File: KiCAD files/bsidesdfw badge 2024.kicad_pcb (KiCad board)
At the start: 2 copper layers, 117.4 x 117.4 mm, 29 parts, among them Q1 BC548, SW1 SW_SPDT_312, U1 NE555P, U2 74HC595

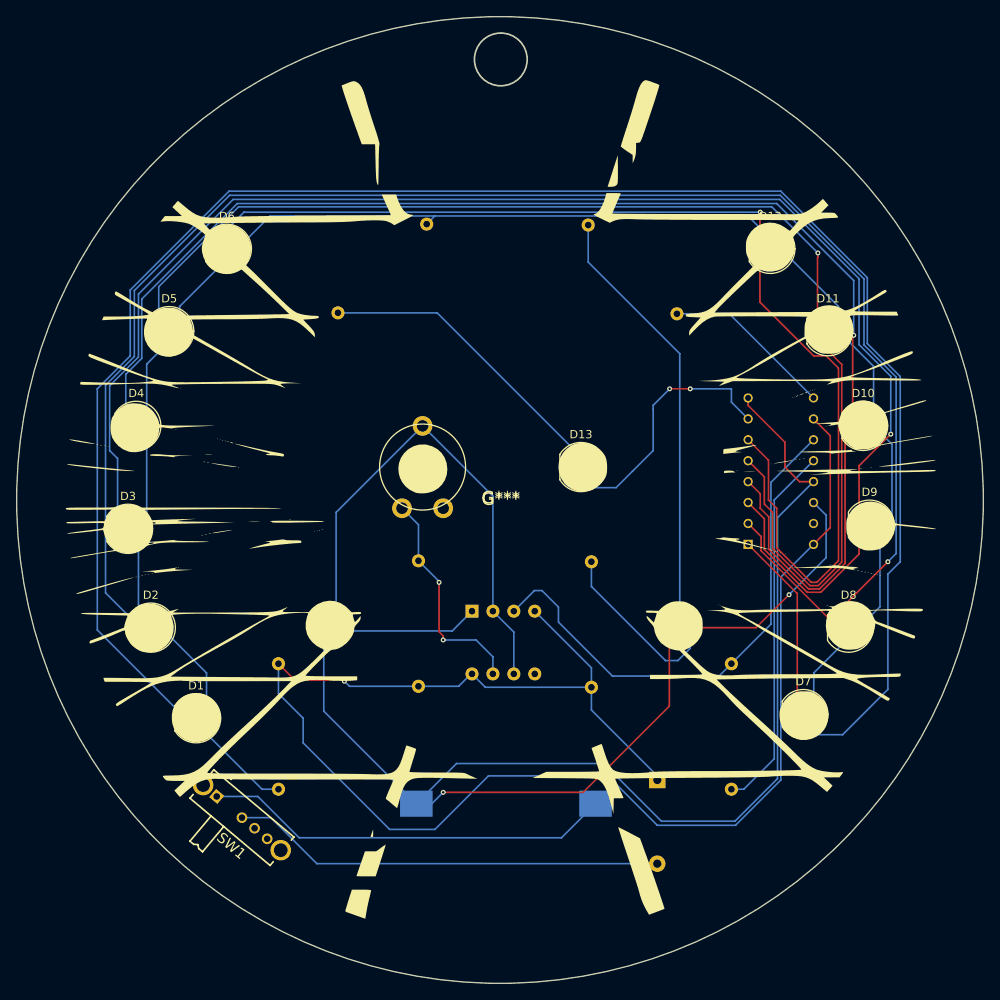
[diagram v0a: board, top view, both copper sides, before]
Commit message: gerbers for PCBWay; Added BSides Logo and website; added silkscreen credits for badge contributors. Moved LED footprints to back of board to address silkscreen conflicts, details are in the README.md
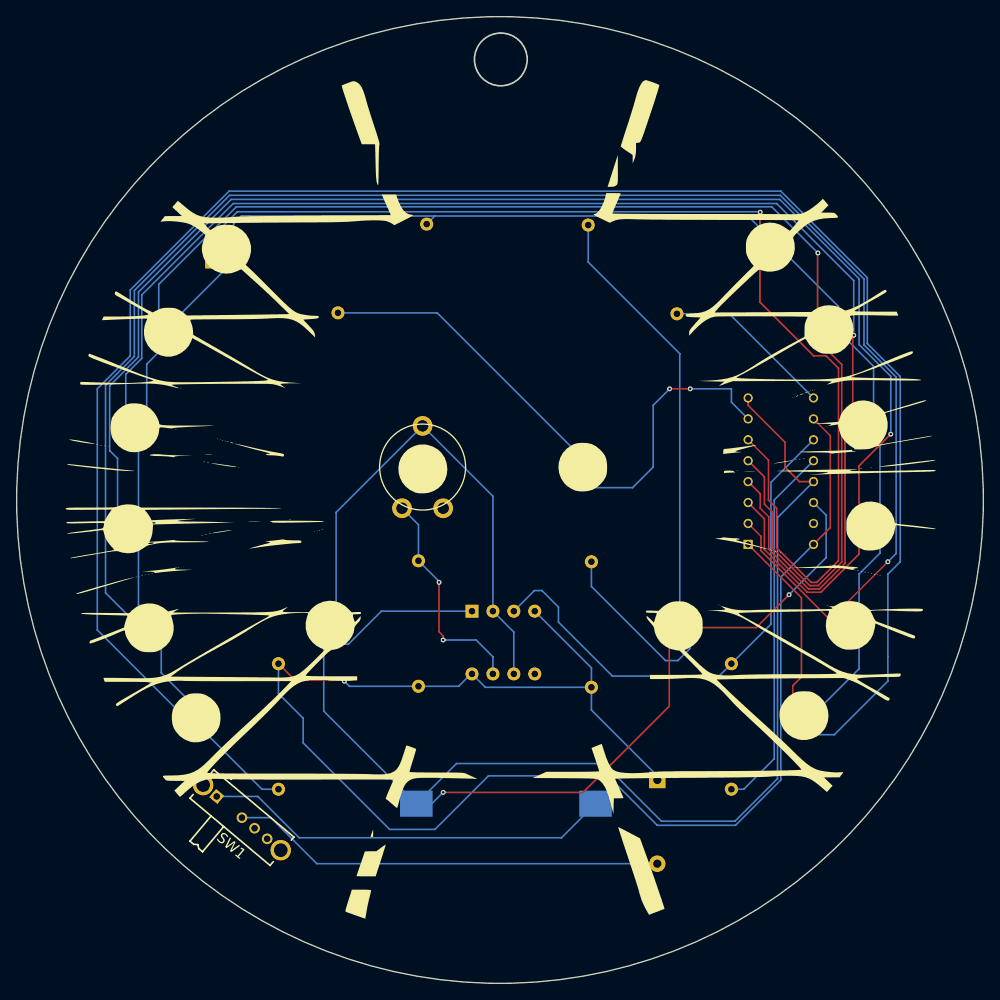
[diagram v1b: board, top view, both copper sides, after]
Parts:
- added G***: LOGO, hon1nbo-library:bsides-logo, B.Cu at (138.0, 50.5)
- added G***: LOGO, hon1nbo-library:hon1nbo-soberdogs-art, B.Cu at (106.5, 91.5)
- D1, D10, D11, D12, D13, D2, D3, D4, D5, D6, D7, D8, D9: moved to B.Cu
- moved D6 1.57 mm to (102.5, 67.5)
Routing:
- net Net-(D12-K): track 140.6 -> 142.8 mm
- net Net-(D13-K): track 33.8 -> 34.4 mm
- net Net-(D1-A): track 215.8 -> 216.4 mm
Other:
- board text added: "Design: ibi5 Masking: bearsinports Electrical & PCB: hon1nbo"
- board text added: "https://bsidesdfw.com/"

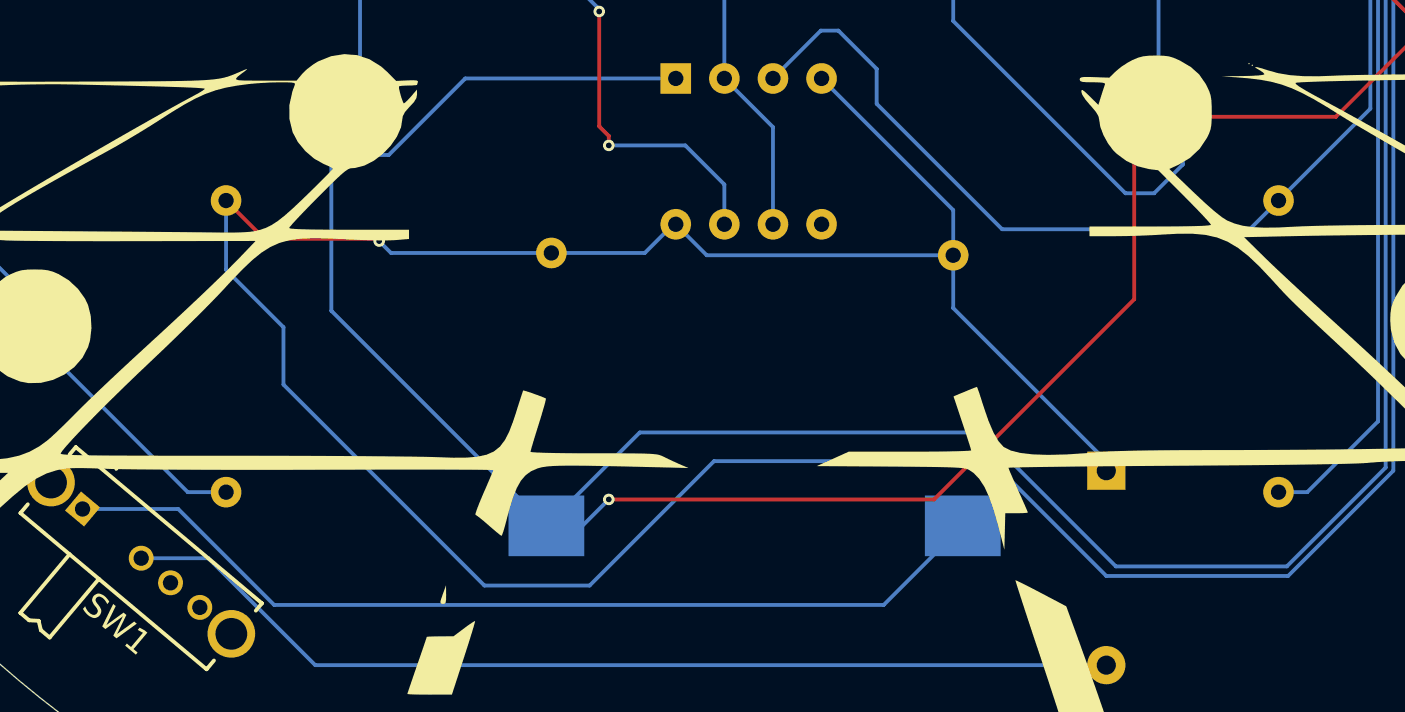
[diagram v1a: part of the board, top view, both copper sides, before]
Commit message: prototype badge tested after delivery; to make assembly easier for first timers increasing pad size for battery clip. Adding larger + indicators for some components. Generated new Gerbers
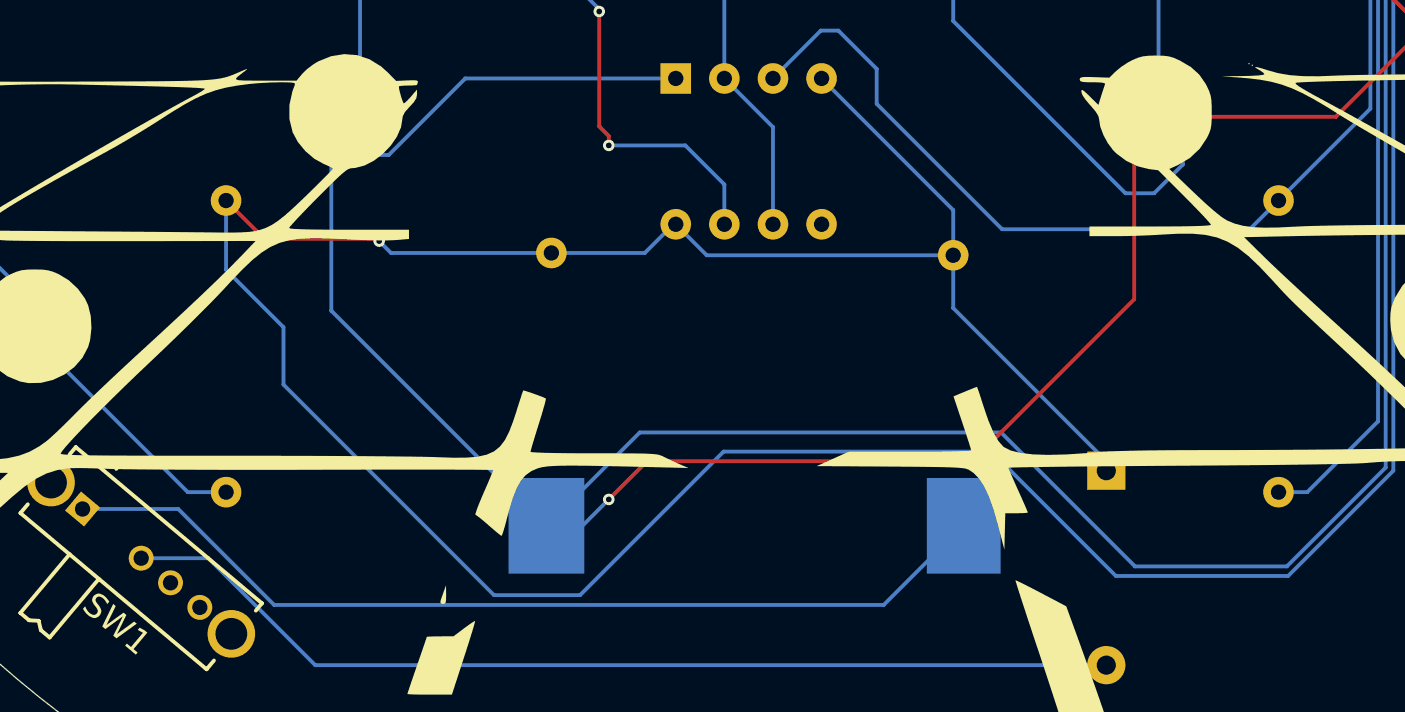
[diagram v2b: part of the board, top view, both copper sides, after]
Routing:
- net +6V: track 194.9 -> 195.8 mm
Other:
- board text added: "+"

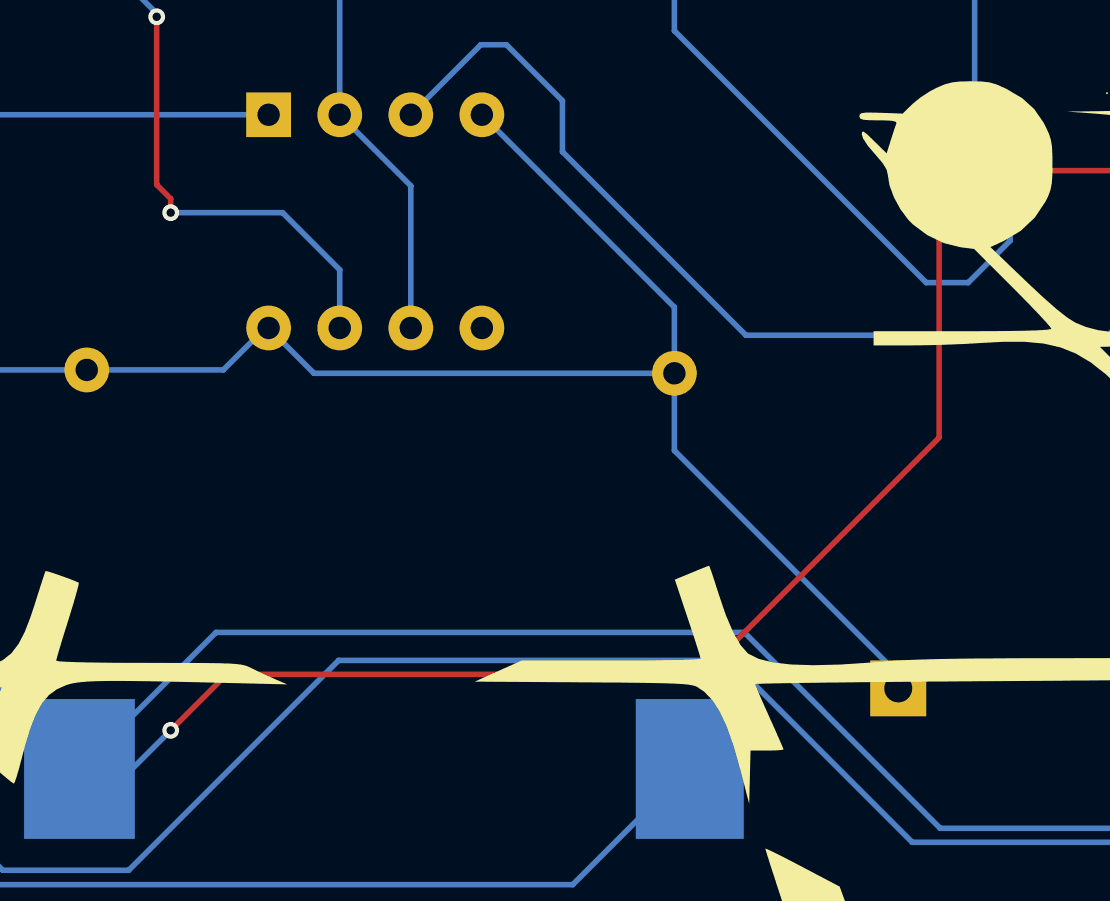
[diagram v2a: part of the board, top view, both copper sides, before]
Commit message: fixed a trace exposure from resizing battery pads; cleaned up and exported schematic to SVG for documentation.
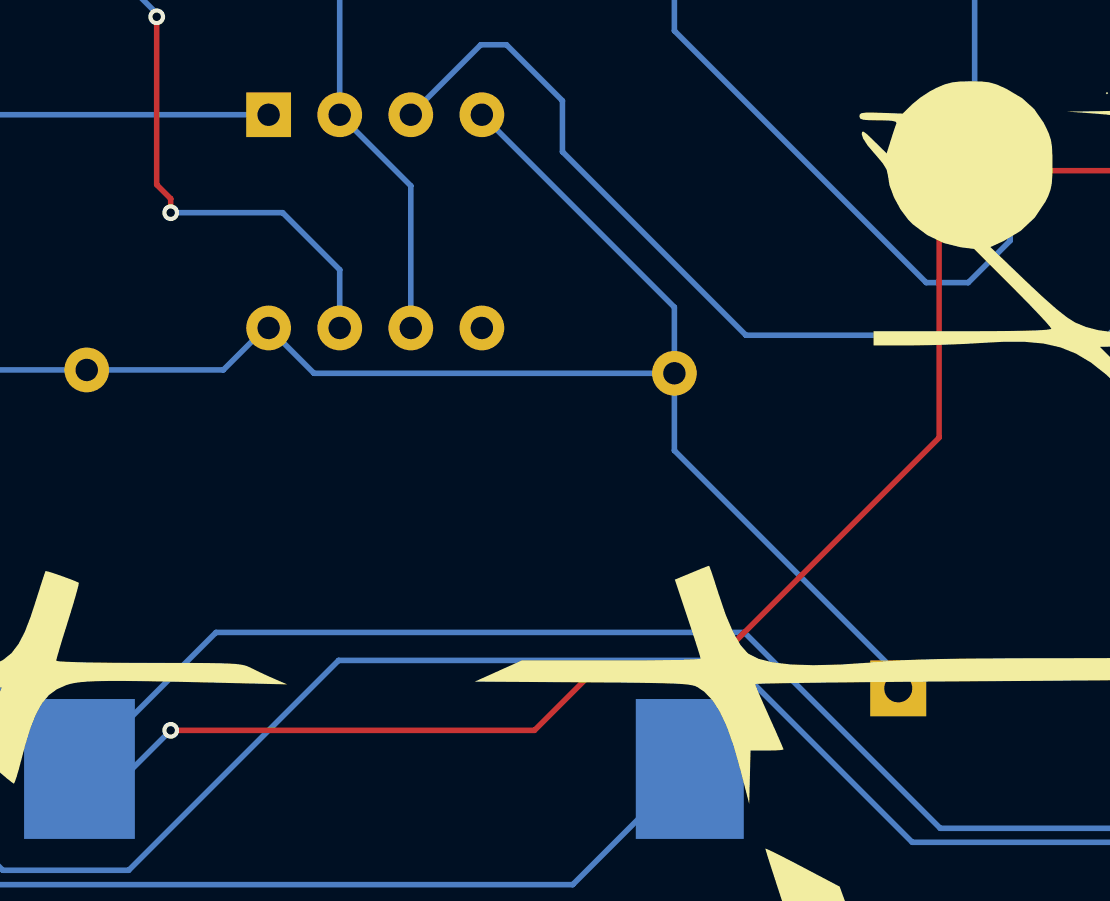
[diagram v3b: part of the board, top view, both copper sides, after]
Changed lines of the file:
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@@
 		(fp_arc
 			(start 0.000001 -2.799999)
-			(mid 0.049998 -2.75)
+			(mid 0.049997 -2.75)
 			(end 0.000001 -2.700001)
 			(stroke
@@
 	)
 	(segment
+		(start 130.5 132)
+		(end 143.5 132)
+		(width 0.2)
+		(layer "F.Cu")
+		(net 1)
+	)
+	(segment
 		(start 172 92.5)
 		(end 173.77 94.27)
@@
 	)
 	(segment
+		(start 145.5 130)
+		(end 149.5 130)
+		(width 0.2)
+		(layer "F.Cu")
+		(net 1)
+	)
+	(segment
 		(start 167.53 84.11)
 		(end 167.53 85.013295)
@@
 	(segment
 		(start 149.5 130)
-		(end 132.5 130)
+		(end 157.96 121.54)
 		(width 0.2)
 		(layer "F.Cu")
@@
 	)
 	(segment
-		(start 173.77 94.27)
-		(end 175.47 94.27)
+		(start 143.5 132)
+		(end 145.5 130)
 		(width 0.2)
 		(layer "F.Cu")
@@
 	)
 	(segment
-		(start 157.96 112)
-		(end 157.96 121.54)
+		(start 173.77 94.27)
+		(end 175.47 94.27)
 		(width 0.2)
 		(layer "F.Cu")
@@
 	(segment
 		(start 157.96 121.54)
-		(end 149.5 130)
-		(width 0.2)
-		(layer "F.Cu")
-		(net 1)
-	)
-	(segment
-		(start 132.5 130)
-		(end 130.5 132)
+		(end 157.96 112)
 		(width 0.2)
 		(layer "F.Cu")

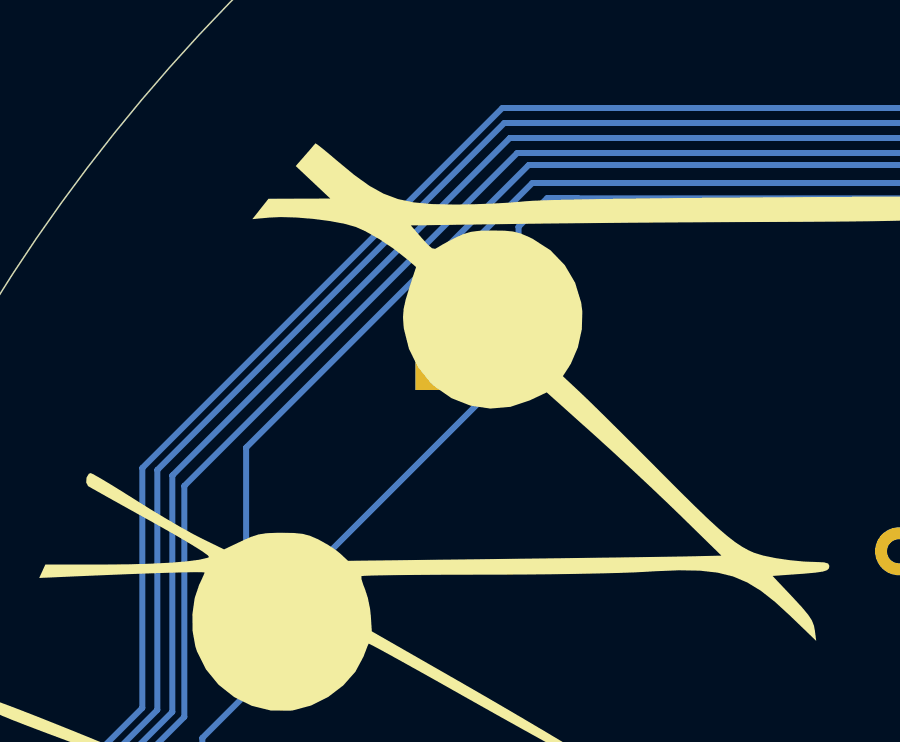
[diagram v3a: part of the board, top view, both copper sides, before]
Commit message: Errata; cleaned up explanations and some other readme stuff
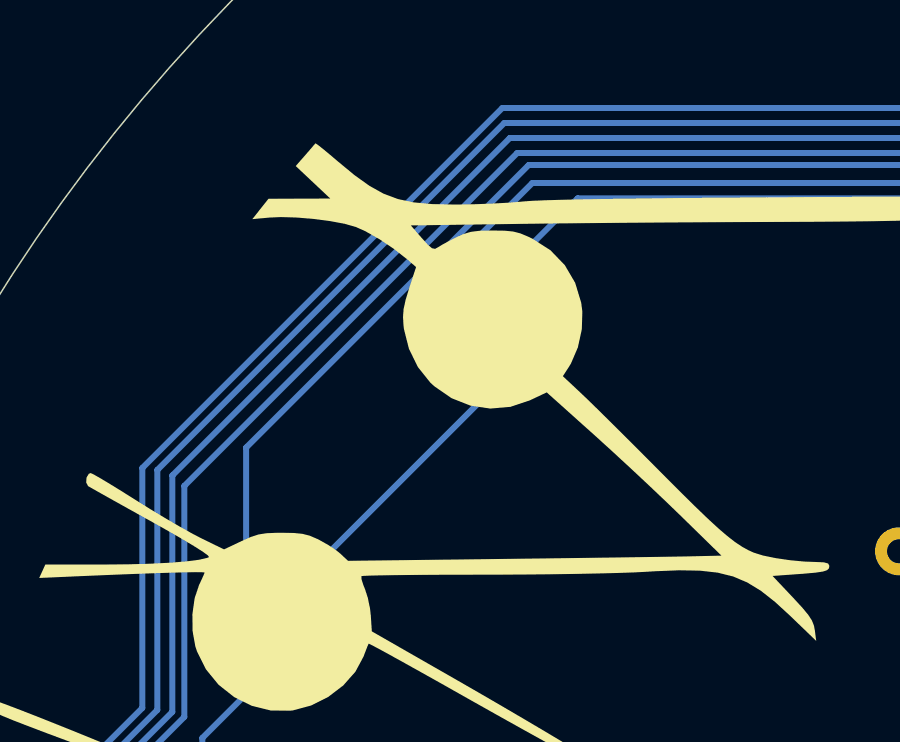
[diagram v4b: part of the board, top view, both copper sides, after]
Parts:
- moved D6 1.58 mm to (103.0, 66.0)
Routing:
- net Net-(D12-K): track 142.8 -> 141.1 mm
- net Net-(D1-A): track 216.4 -> 215.8 mm
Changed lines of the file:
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@@
 		(fp_arc
 			(start 0.000001 -2.799999)
-			(mid 0.049997 -2.75)
+			(mid 0.049996 -2.75)
 			(end 0.000001 -2.700001)
 			(stroke
@@
 	(footprint "LED_THT:LED_D5.0mm"
 		(layer "B.Cu")
-		(at 102.5 67.5)
+		(at 103 66)
 		(descr "LED, diameter 5.0mm, 2 pins, http://cdn-reichelt.de/documents/datenblatt/A500/LL-504BC2E-009.pdf")
 		(tags "LED diameter 5.0mm 2 pins")
@@
 	)
 	(segment
-		(start 105.04 67.5)
-		(end 105.04 62.96)
+		(start 98.5 74.04)
+		(end 105.54 67)
 		(width 0.2)
 		(layer "B.Cu")
@@
 	)
 	(segment
-		(start 98.5 74.04)
-		(end 105.04 67.5)
+		(start 107.011847 62.011847)
+		(end 105.54 63.483694)
 		(width 0.2)
 		(layer "B.Cu")
@@
 	)
 	(segment
-		(start 107.011847 62.011847)
-		(end 129.5 62.011847)
-		(width 0.2)
-		(layer "B.Cu")
-		(net 11)
-	)
-	(segment
 		(start 183.54 99.5)
 		(end 183.54 88.275)
@@
 	)
 	(segment
-		(start 107 62)
-		(end 107.011847 62.011847)
+		(start 105.54 63.483694)
+		(end 105.54 66)
 		(width 0.2)
 		(layer "B.Cu")
@@
 	)
 	(segment
-		(start 181 105.5)
-		(end 183.54 102.96)
+		(start 107.011847 62.011847)
+		(end 129.5 62.011847)
 		(width 0.2)
 		(layer "B.Cu")
@@
 	)
 	(segment
-		(start 94.5 87.5)
-		(end 94.5 80)
+		(start 181 105.5)
+		(end 183.54 102.96)
 		(width 0.2)
 		(layer "B.Cu")
@@
 	)
 	(segment
-		(start 105.04 62.96)
-		(end 106 62)
+		(start 94.5 87.5)
+		(end 94.5 80)
 		(width 0.2)
 		(layer "B.Cu")
@@
 	)
 	(segment
-		(start 167.511847 62.011847)
-		(end 171.5 66)
+		(start 105.54 67)
+		(end 105.54 66)
 		(width 0.2)
 		(layer "B.Cu")
@@
 	)
 	(segment
-		(start 106 62)
-		(end 107 62)
+		(start 167.511847 62.011847)
+		(end 171.5 66)
 		(width 0.2)
 		(layer "B.Cu")
@@
 	)
 	(segment
-		(start 105.5 61.5)
-		(end 168.95 61.5)
+		(start 103 66)
+		(end 103 64)
 		(width 0.2)
 		(layer "B.Cu")
@@
 	)
 	(segment
-		(start 168.95 61.5)
-		(end 169 61.55)
+		(start 105.5 61.5)
+		(end 168.95 61.5)
 		(width 0.2)
 		(layer "B.Cu")
@@
 	)
 	(segment
-		(start 102.5 67.5)
-		(end 102.5 64.5)
+		(start 103 64)
+		(end 105.5 61.5)
 		(width 0.2)
 		(layer "B.Cu")
@@
 	)
 	(segment
-		(start 102.5 64.5)
-		(end 105.5 61.5)
+		(start 168.95 61.5)
+		(end 169 61.55)
 		(width 0.2)
 		(layer "B.Cu")
